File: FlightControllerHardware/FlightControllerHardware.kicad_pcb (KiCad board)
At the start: 2 copper layers, 21 parts, among them J1 Power in, J2 Power in, J3 servoRight, J4 servoBack, J5 servoLeft, J6 servoFront, J7 mainThrust, SW1 SW_Push, U1 module_bme280, U2 Pico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

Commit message: finished routing
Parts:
- added J8: mainThrust, Connector_JST:JST_EH_B2B-EH-A_1x02_P2.50mm_Vertical, F.Cu at (131.3, 70.6)
- J3: value servoRight -> Conn_01x20_Male; footprint Connector_JST:JST_EH_B4B-EH-A_1x04_P2.50mm_Vertical -> Connector_PinHeader_2.54mm:PinHeader_1x20_P2.54mm_Vertical
- J4: value servoBack -> servoRight
- J5: value servoLeft -> servoBack
- J6: value servoFront -> servoLeft
- J7: value mainThrust -> servoFront; footprint Connector_JST:JST_EH_B2B-EH-A_1x02_P2.50mm_Vertical -> Connector_JST:JST_EH_B4B-EH-A_1x04_P2.50mm_Vertical
- moved J1 221.0 mm to (229.8, 85.3), turned to -90 degrees
- moved J2 212.1 mm to (229.8, 92.5), turned to -90 degrees
- moved U3 209.1 mm to (221.6, 86.1), turned to -90 degrees
- moved U6 202.3 mm to (221.3, 73.3), turned to -90 degrees
- moved C2 199.8 mm to (215.8, 78.9), turned to 180 degrees
- moved C3 189.5 mm to (208.9, 85.3)
- moved C1 187.0 mm to (209.4, 90.5), turned to 0 degrees
- moved C4 183.3 mm to (208.4, 74.1), turned to 0 degrees
- moved U5 174.0 mm to (214.3, 110.2), turned to 0 degrees
- moved J3 170.5 mm to (192.0, 122.5), turned to 180 degrees
- moved R2 119.3 mm to (158.9, 122.6), turned to 180 degrees
- moved R1 118.2 mm to (150.6, 122.4), turned to 180 degrees
- moved J4 116.4 mm to (121.0, 71.0), turned to -90 degrees
- moved U1 100.4 mm to (149.6, 104.5)
- moved J5 92.7 mm to (121.1, 86.1), turned to -90 degrees
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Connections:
- J3 pad 1: servoRight -> gpsRx
- J3 pad 2: servoRight -> gpsTx
- J3 pad 3: +5V -> Net-(J3-Pad3)
- J3 pad 4: GND -> Net-(J3-Pad4)
- J4 pad 1: servoBack -> servoRight
- J4 pad 2: servoBack -> servoRight
- J5 pad 1: servoLeft -> servoBack
- J5 pad 2: servoLeft -> servoBack
- J6 pad 1: servoFront -> servoLeft
- J6 pad 2: servoFront -> servoLeft
- J7 pad 1: mainThrust -> servoFront
- J7 pad 2: GND -> servoFront
- SW1 pad 1: Net-(SW1-Pad1) -> Net-(J3-Pad10)
- SW1 pad 2: Net-(SW1-Pad2) -> Net-(J3-Pad8)
- U2 pad 1: gpsRx -> unconnected-(U2-Pad1)
- U2 pad 13: GND -> unconnected-(U2-Pad13)
- U2 pad 2: gpsTx -> unconnected-(U2-Pad2)
- U2 pad 21: unconnected-(U2-Pad21) -> gpsRx
- U2 pad 22: unconnected-(U2-Pad22) -> gpsTx
- U2 pad 23: unconnected-(U2-Pad23) -> Net-(J3-Pad3)
- U2 pad 24: unconnected-(U2-Pad24) -> Net-(J3-Pad4)
- U2 pad 25: unconnected-(U2-Pad25) -> Net-(J3-Pad5)
- U2 pad 26: unconnected-(U2-Pad26) -> Net-(J3-Pad6)
- U2 pad 27: unconnected-(U2-Pad27) -> Net-(J3-Pad7)
- U2 pad 28: Net-(SW1-Pad2) -> Net-(J3-Pad8)
- U2 pad 29: unconnected-(U2-Pad29) -> Net-(J3-Pad9)
- U2 pad 30: Net-(SW1-Pad1) -> Net-(J3-Pad10)
- U2 pad 31: unconnected-(U2-Pad31) -> Net-(J3-Pad11)
- U2 pad 32: unconnected-(U2-Pad32) -> Net-(J3-Pad12)
- U2 pad 33: unconnected-(U2-Pad33) -> Net-(J3-Pad13)
- U2 pad 34: unconnected-(U2-Pad34) -> Net-(J3-Pad14)
- U2 pad 35: unconnected-(U2-Pad35) -> Net-(J3-Pad15)
- U2 pad 37: unconnected-(U2-Pad37) -> Net-(J3-Pad17)
- U2 pad 38: unconnected-(U2-Pad38) -> Net-(J3-Pad18)
- U2 pad 39: unconnected-(U2-Pad39) -> Net-(J3-Pad19)
- U2 pad 40: unconnected-(U2-Pad40) -> Net-(J3-Pad20)
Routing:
- net GND: track 0.00 -> 496.4 mm, vias 0 -> 1
- net +5V: track 0.00 -> 216.6 mm
- net +3V3: track 0.00 -> 165.1 mm
- net servoRight: track 0.00 -> 77.1 mm
- net mainThrust: track 0.00 -> 76.6 mm
- net servoFront: track 0.00 -> 66.0 mm
- net servoBack: track 0.00 -> 66.0 mm
- net servoLeft: track 0.00 -> 57.0 mm
- net loraRst: track 0.00 -> 55.0 mm
- net I2C_SDA: track 0.00 -> 51.6 mm
- net I2C_SCL: track 0.00 -> 49.7 mm
- net loraDio0: track 0.00 -> 43.2 mm
- net loraDio1: track 0.00 -> 43.1 mm
- net Net-(J3-Pad8): track 0.00 -> 28.3 mm
- net loraNss: track 0.00 -> 28.2 mm
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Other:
- board outline added: 120.3 x 62.6 mm

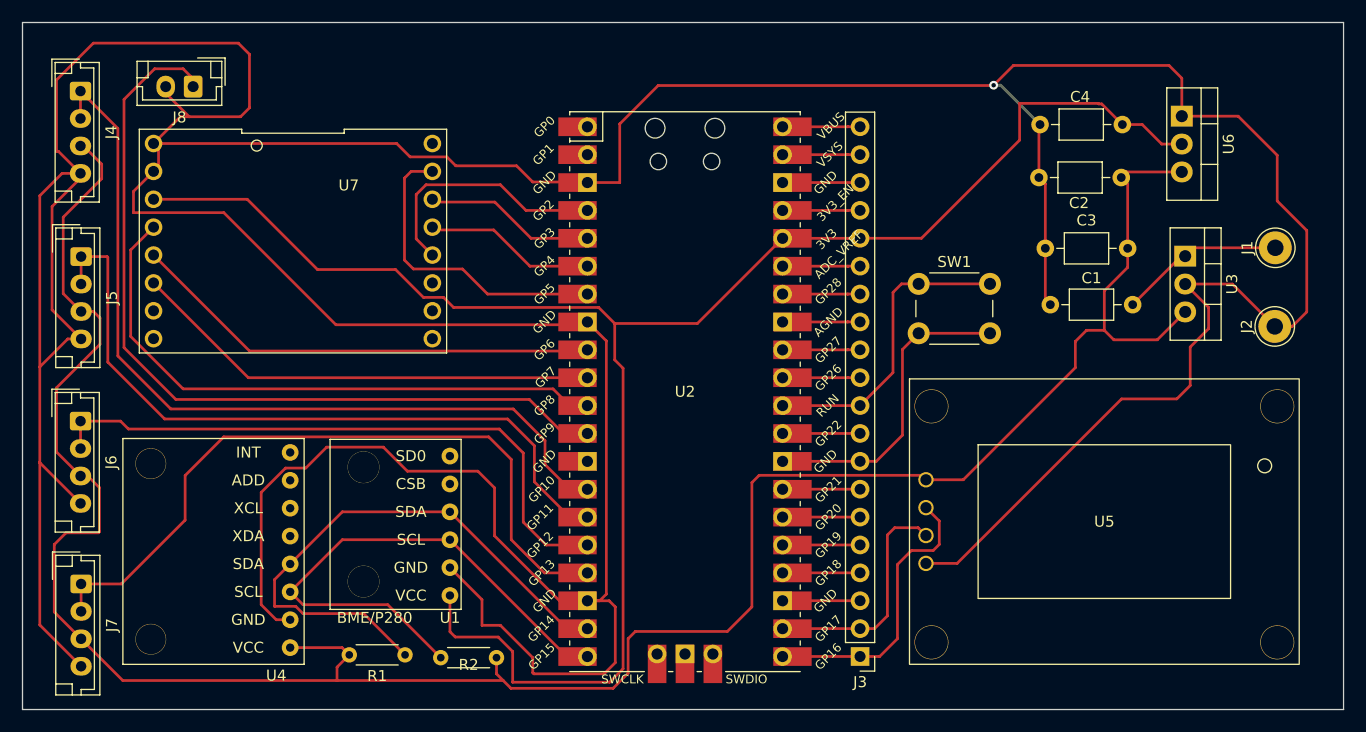
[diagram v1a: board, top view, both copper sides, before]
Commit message: updated pcb to backtraces and removed vias
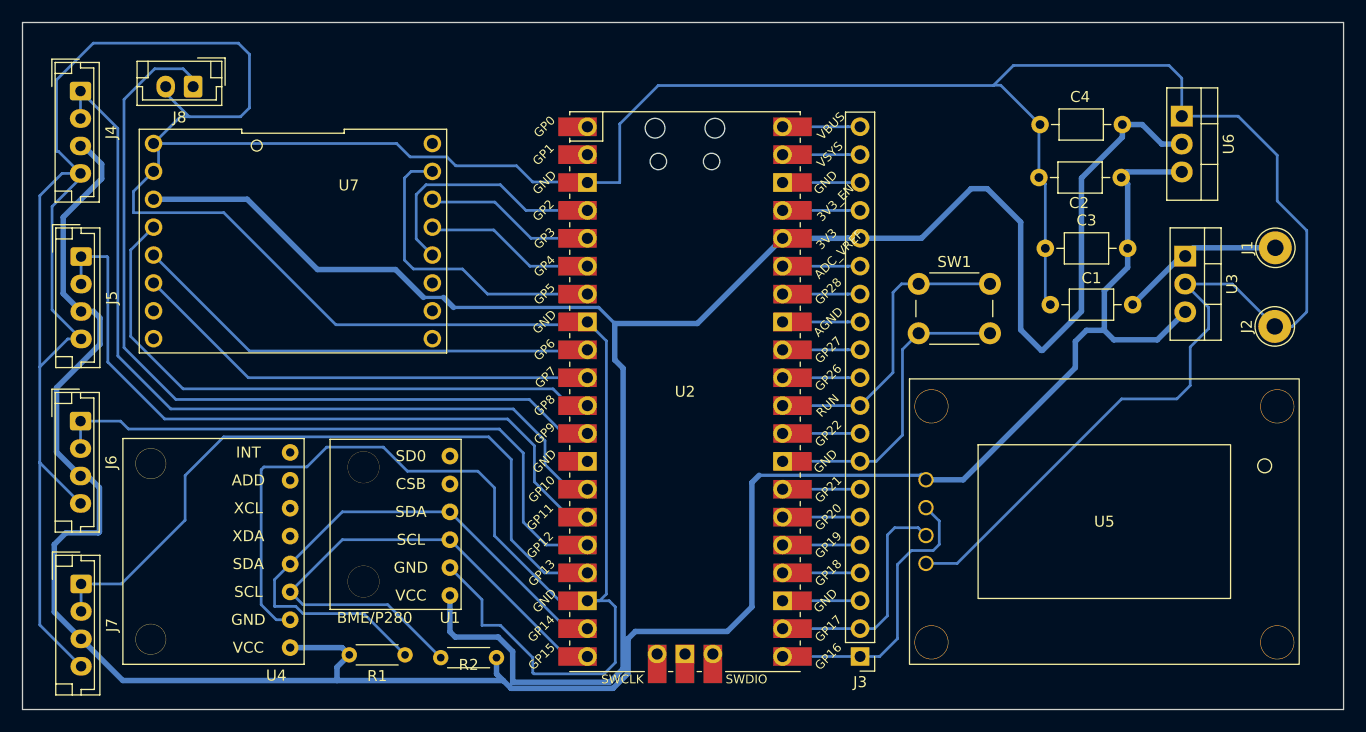
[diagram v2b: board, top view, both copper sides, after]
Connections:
- C2 pad 1: +5V -> +3V3
- C3 pad 2: +5V -> +3V3
- J4 pad 3: +5V -> +3V3
- J5 pad 3: +5V -> +3V3
- J6 pad 3: +5V -> +3V3
- J7 pad 3: +5V -> +3V3
- R1 pad 2: +5V -> +3V3
- R2 pad 1: +5V -> +3V3
- U3 pad 3: +5V -> +3V3
- U4 pad 1: +5V -> +3V3
- U5 pad 1: +5V -> +3V3
- U6 pad 3: +5V -> +3V3
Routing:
- net +3V3: track 165.1 -> 403.8 mm
- net +5V: track 216.6 -> 0.00 mm
- net GND: track 496.4 -> 497.6 mm, vias 1 -> 0
